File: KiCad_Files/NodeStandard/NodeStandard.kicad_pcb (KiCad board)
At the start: 2 copper layers, 129 x 170.6 mm, 123 parts, among them J1 AC Current In, J10 Opto Coupler 1 in, J11 Opto Coupler 2 in, J12 Opto Coupler 3 in, J13 Relay 1 Output, J14 Relay 2 Output, J15 Switch 3 in, J16 Switch 2 in, J17 Switch 1 in, J18 Force output FET 1 on, J19 Force output FET 2 on, J2 Current coil in, J20 FET 1 Output, J21 FET 2 Output, J22 Force output Relay 3 on, J23 Relay 3 Output 1, J24 Relay 3 Output 2, J25 230VAC/12-40VDC in, J26 5V-in, J27 ExtDC-in, J28 Hal current sensor, J29 Current sensor select, J3 AC Current loop, J4 EXT1, J5 OledDisplay, J6 RFIDReader, J7 EXT2, J8 Force output Relay 1 on, J9 Force output Relay 2 on, K1 SANYOU_SRD_Form_C, K2 SANYOU_SRD_Form_C, K3 RT42xAxx, Q1 BC547, Q2 BC547, Q3 IRLZ34N, Q4 IRLZ34N, Q5 BC547, Q6 2N3906, U1 MCP23017_SP

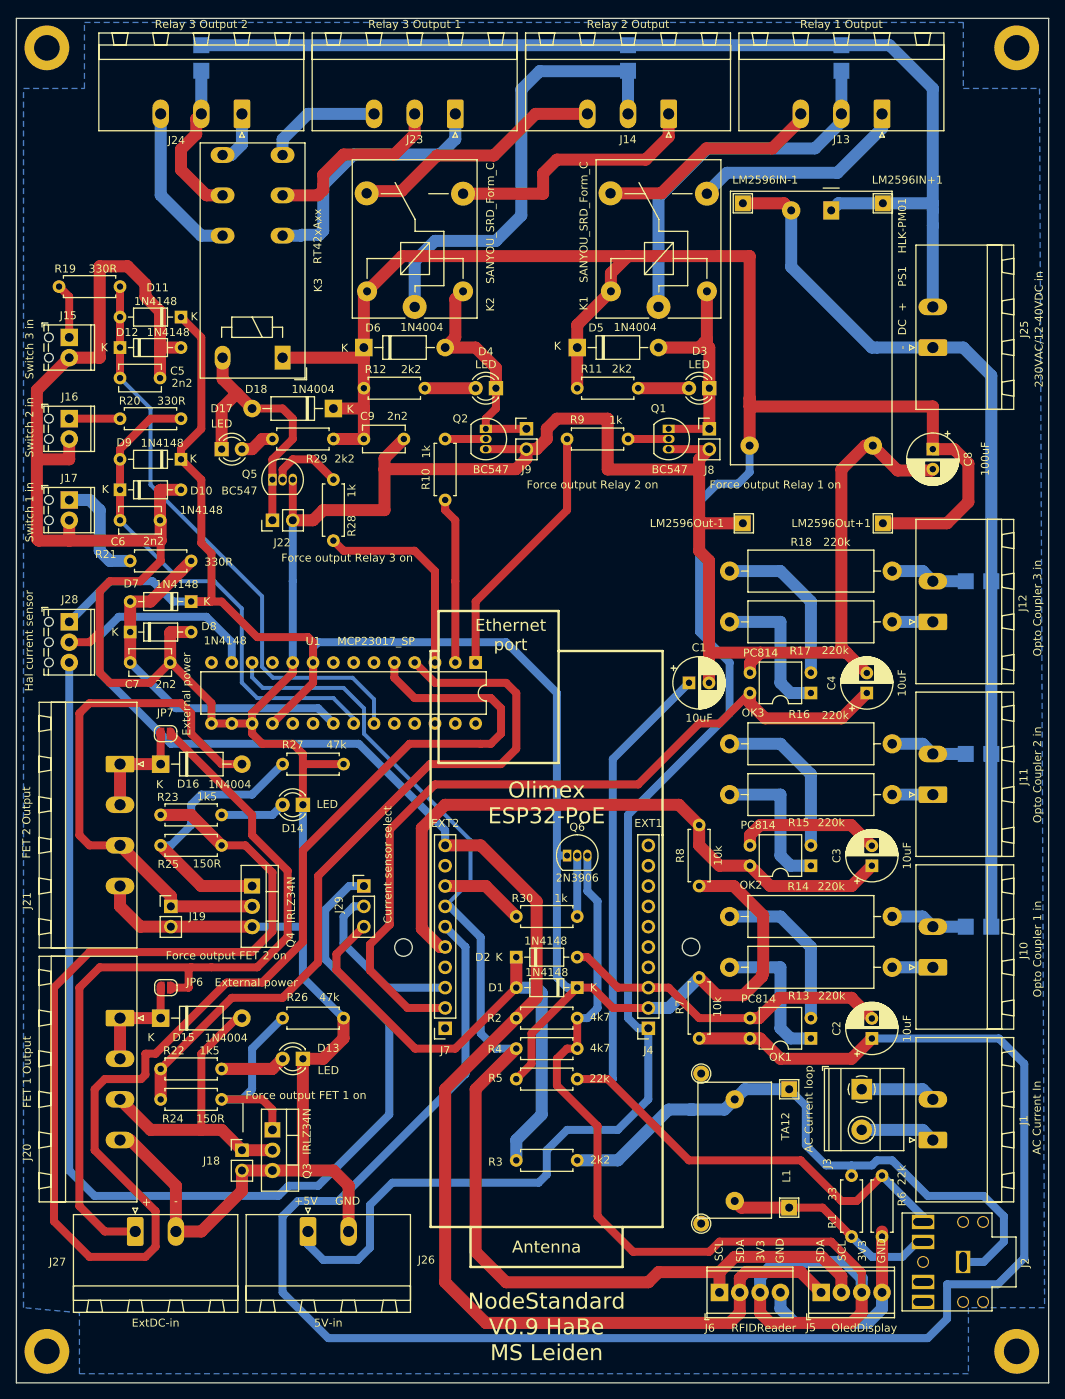
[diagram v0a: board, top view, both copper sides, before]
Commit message: Third (fysical) version of the PCB for this node. Added a header to provide access to some free (currently not used GPIO ports), also made the holes for the coil a little bit wider
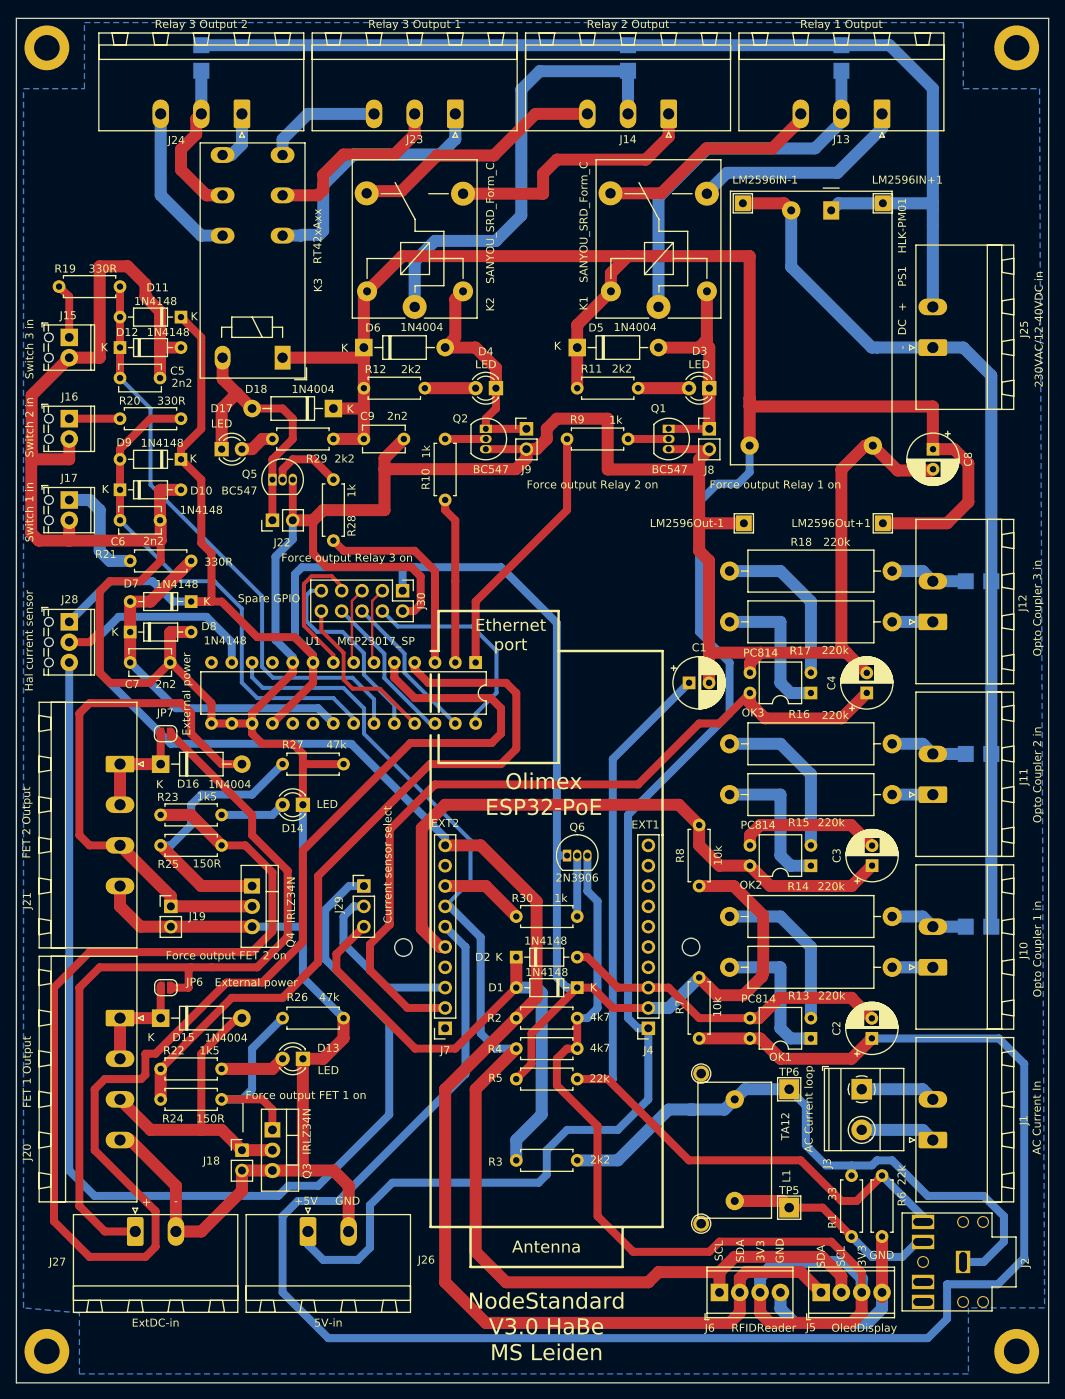
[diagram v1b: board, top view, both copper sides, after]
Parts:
- added J30: Spare GPIO, Connector_PinHeader_2.54mm:PinHeader_2x05_P2.54mm_Vertical, F.Cu at (74.1, 93.3)
- TP5, TP6: footprint TestPoint:TestPoint_THTPad_2.0x2.0mm_Drill1.0mm -> TestPoint:TestPoint_THTPad_2.5x2.5mm_Drill1.2mm
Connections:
- J2 pad R: (no net) -> unconnected-(J2-PadR)
- J2 pad RN: (no net) -> unconnected-(J2-PadRN)
- J4 pad 10: (no net) -> unconnected-(J4-Pad10)
- J4 pad 4: (no net) -> unconnected-(J4-Pad4)
- J4 pad 5: (no net) -> unconnected-(J4-Pad5)
- J4 pad 6: (no net) -> unconnected-(J4-Pad6)
- J4 pad 7: (no net) -> unconnected-(J4-Pad7)
- J4 pad 8: (no net) -> unconnected-(J4-Pad8)
- J4 pad 9: (no net) -> unconnected-(J4-Pad9)
- J7 pad 1: (no net) -> GPI39
- J7 pad 4: (no net) -> GPI34_BUT1
- J7 pad 9: (no net) -> GPIO14_HS2_CLK
- U1 pad 11: (no net) -> unconnected-(U1-Pad11)
- U1 pad 14: (no net) -> unconnected-(U1-Pad14)
- U1 pad 19: (no net) -> unconnected-(U1-Pad19)
- U1 pad 20: (no net) -> unconnected-(U1-Pad20)
- U1 pad 24: (no net) -> Net-(J30-Pad9)
- U1 pad 25: (no net) -> Net-(J30-Pad10)
- U1 pad 26: (no net) -> Net-(J30-Pad8)
- U1 pad 27: (no net) -> Net-(J30-Pad6)
- U1 pad 28: (no net) -> Net-(J30-Pad4)
- U1 pad 6: (no net) -> Net-(J30-Pad3)
- U1 pad 7: (no net) -> Net-(J30-Pad5)
- U1 pad 8: (no net) -> Net-(J30-Pad7)
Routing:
- net GND: track 598.0 -> 625.9 mm
- net Net-(J30-Pad4): track 0.00 -> 26.5 mm
- net Net-(J30-Pad9): track 0.00 -> 24.6 mm
- net +3V3: track 224.4 -> 247.8 mm
- net Net-(J30-Pad10): track 0.00 -> 20.9 mm
- net Net-(J30-Pad8): track 0.00 -> 19.3 mm
- net Net-(J30-Pad6): track 0.00 -> 18.9 mm
- net Net-(J30-Pad7): track 0.00 -> 17.6 mm
- net Net-(J30-Pad5): track 0.00 -> 9.59 mm
- net Net-(J30-Pad3): track 0.00 -> 9.59 mm
- net FET2: track 219.7 -> 221.0 mm
- net Net-(J2-PadTN): track 28.4 -> 27.5 mm
- net GPIO13_I2C-SDA: track 201.2 -> 200.7 mm
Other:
- net class Default removed
- board text added: "NodeStandard V3.0 HaBe MS Leiden"
- board text removed: "NodeStandard V0.9 HaBe MS Leiden"
